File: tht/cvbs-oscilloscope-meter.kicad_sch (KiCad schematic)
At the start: 54 parts, among them J1 Conn_Coaxial_Power, J2 Conn_Coaxial_Power, J3 Conn_Coaxial_Power, J4 Conn_Coaxial_Power, J5 Barrel_Jack_Switch, J6 Molex 3.96mm, Q1 2N3906, Q2 2N3906, Q3 2N3904, Q4 2N3904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

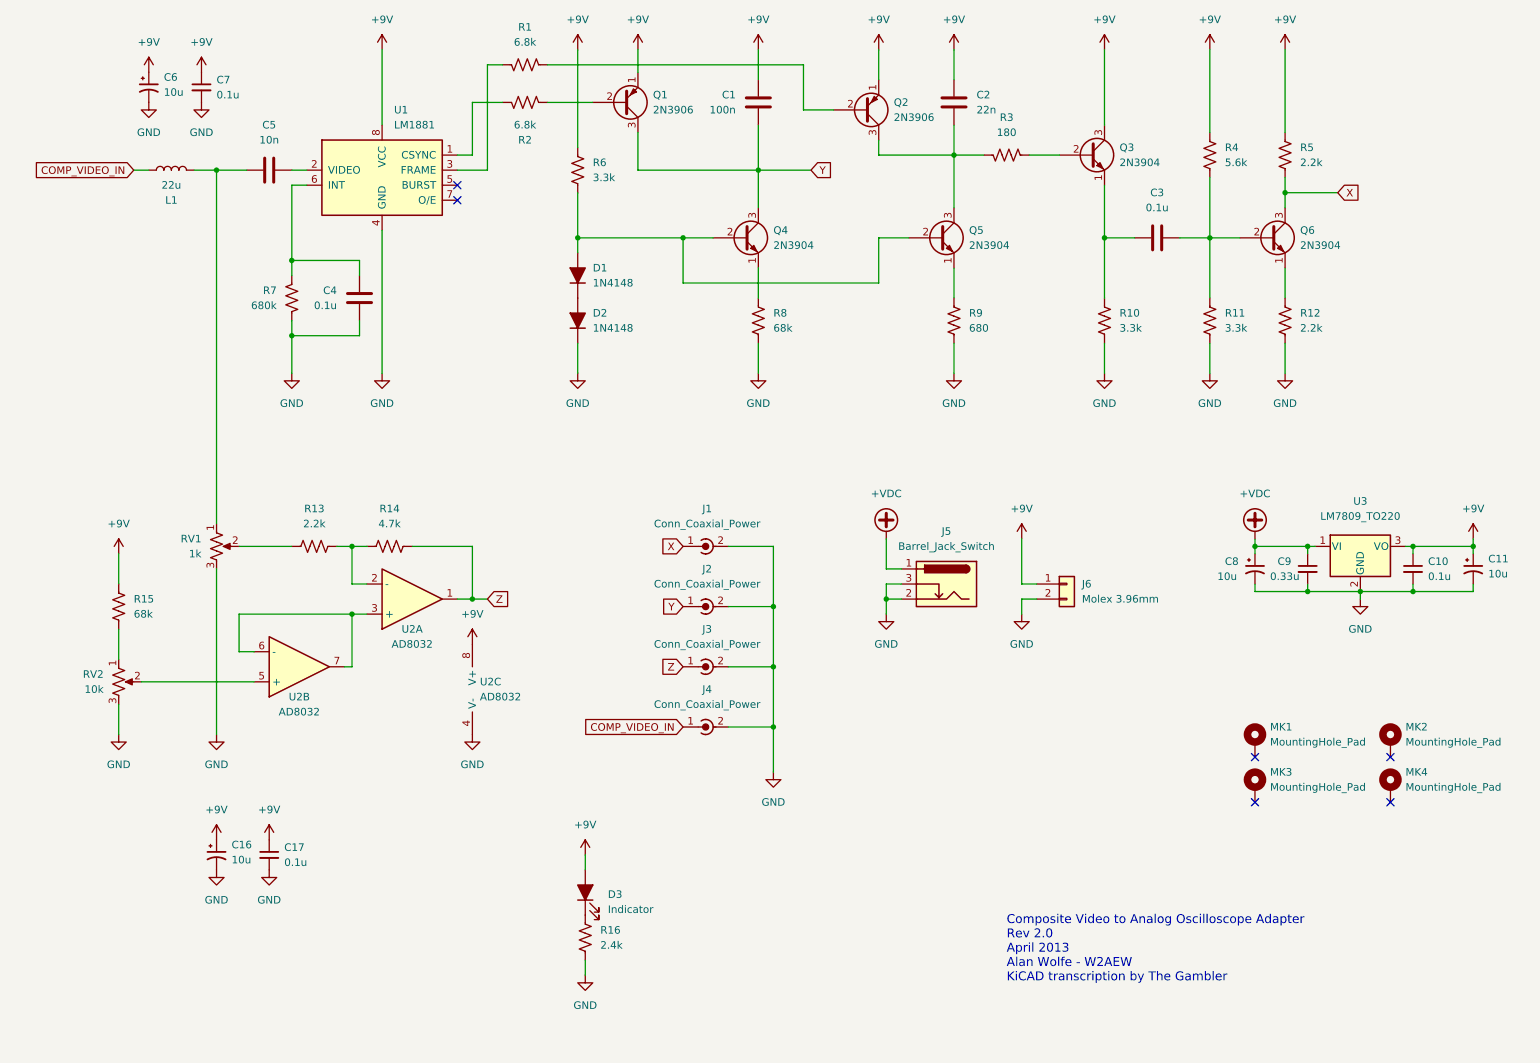
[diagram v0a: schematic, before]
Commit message: Started PCB layout v2
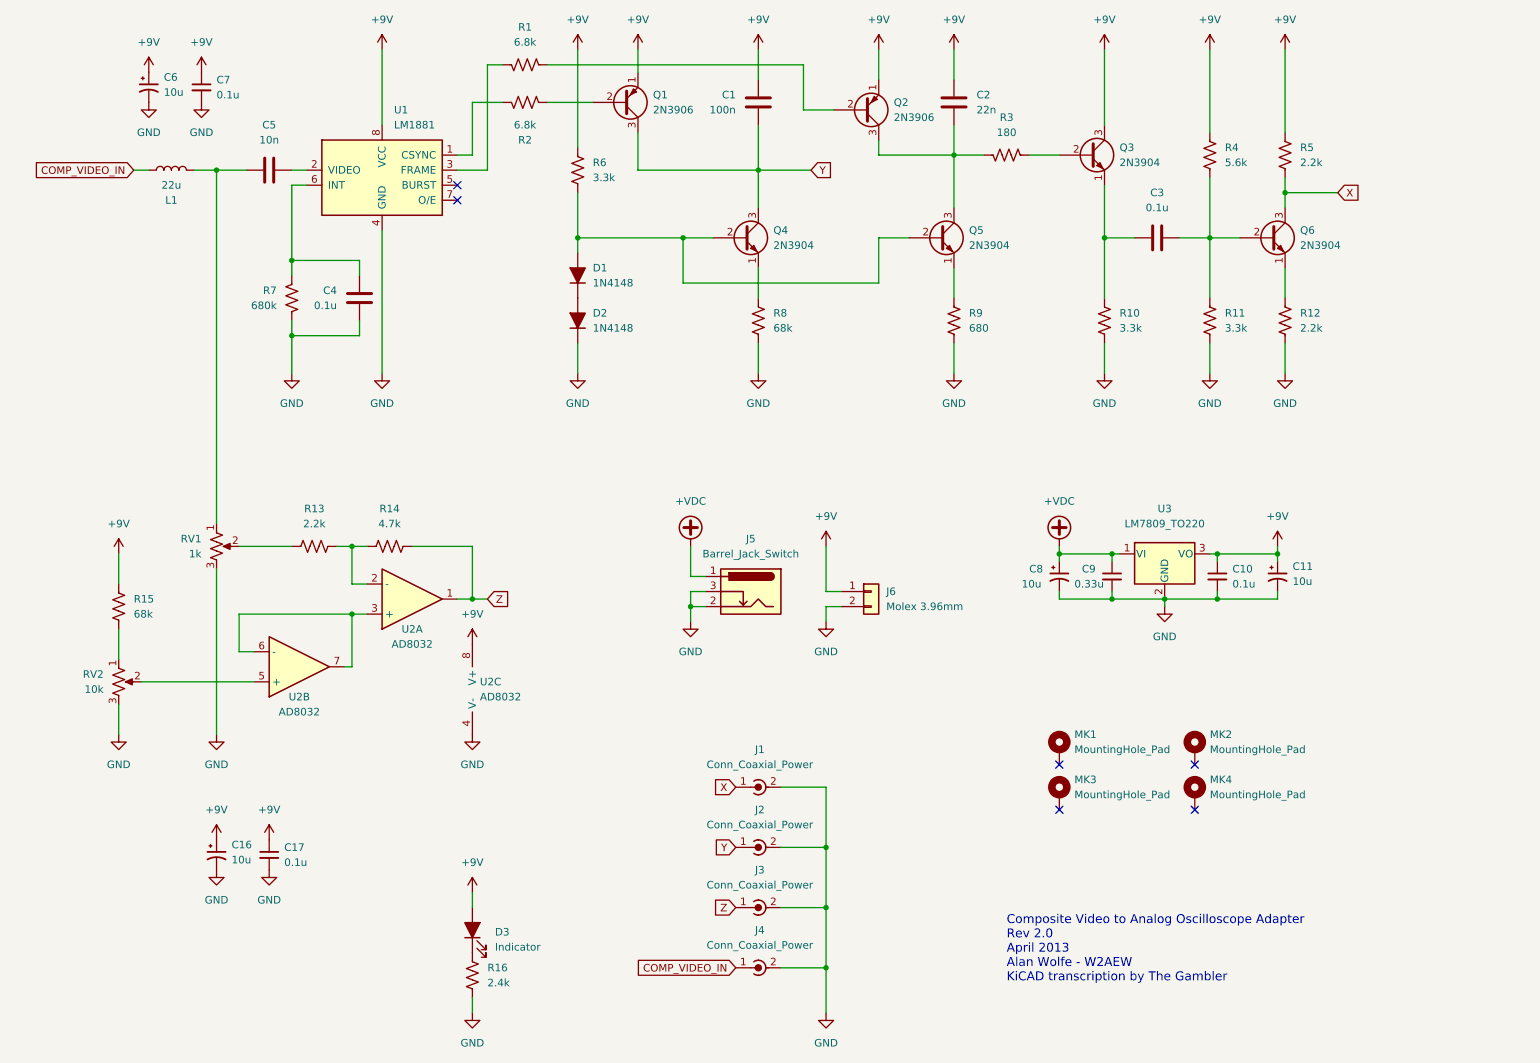
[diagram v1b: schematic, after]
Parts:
- C6: footprint Capacitor_THT:C_Disc_D7.5mm_W2.5mm_P5.00mm -> Capacitor_THT:CP_Radial_D8.0mm_P3.50mm
- J6: footprint Connector_BarrelJack:BarrelJack_CUI_PJ-063AH_Horizontal -> Connector_Molex:Molex_KK-396_A-41791-0002_1x02_P3.96mm_Vertical
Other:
- moved on the sheet: C10, C11, C8, C9, D3, J1, J2, J3, J4, J5, J6, MK1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
